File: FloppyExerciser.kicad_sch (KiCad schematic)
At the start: 112 parts, among them J1 STEPPER, J10 IBM 31SD, J11 PS/2, J12 APPLE II, J2 WRITE, J4 V, J5 ISP, J6 IBM, J7 HP 34-PIN, J8 HP 26-PIN, J9 SHUGART, SW1 RotaryEncoder_Switch, SW10 DIR, SW11 TG43 MODE, SW12 MENU, SW13 DENSITY, SW2 STEP, SW3 DISKCH_RST, SW4 DSEL, SW5 DSEL2, SW6 DRIVE_SELECT, SW7 MOTOR_ON, SW8 HEAD_SEL, SW9 HEAD_LOAD, U1 ATmega328PB-M, U2 74LS245, U3 74LS32, U4 74LS04

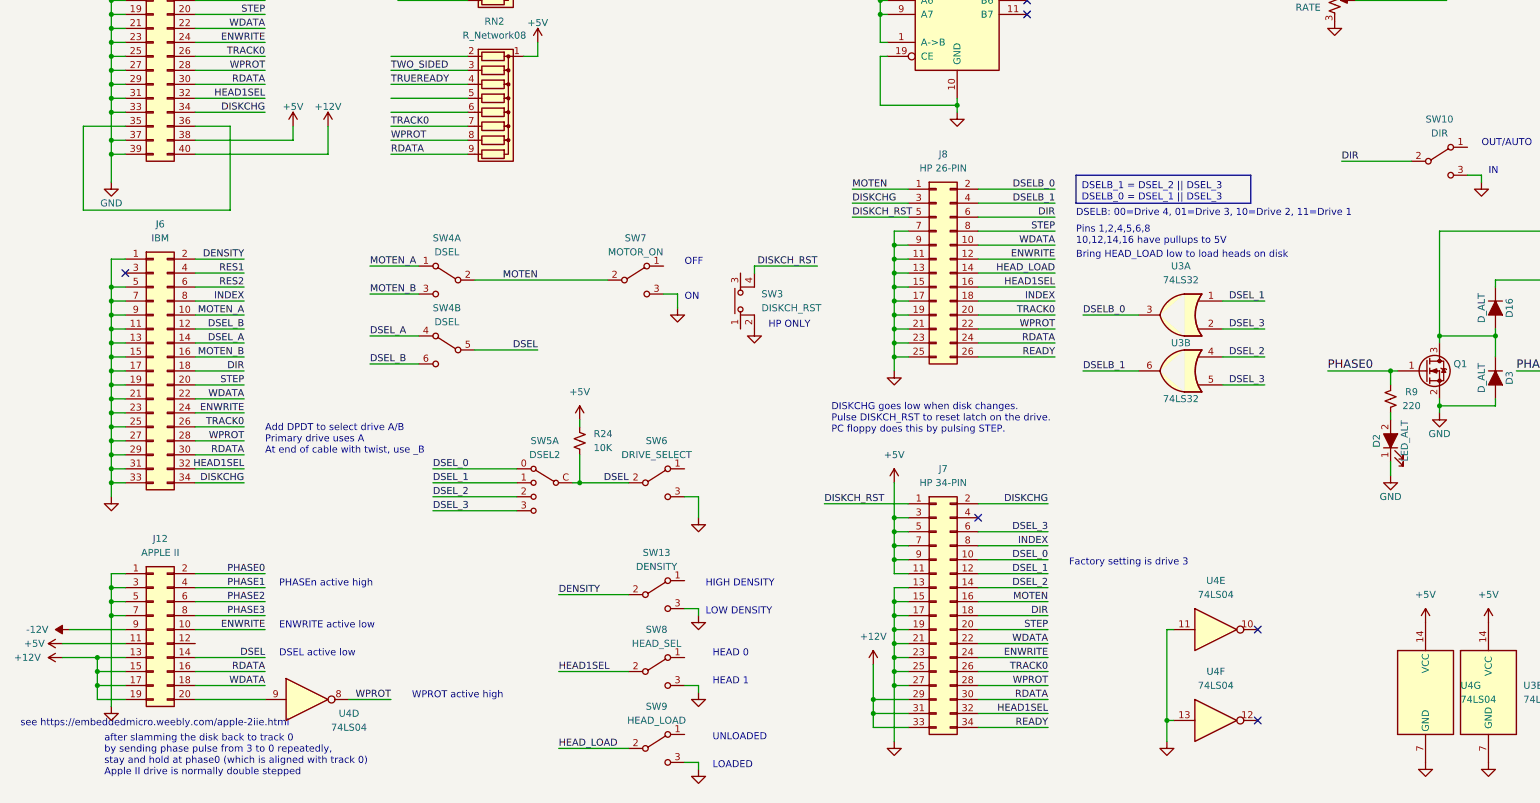
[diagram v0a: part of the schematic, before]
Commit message: Rev2 fab with minor fixes for HP 26 pin
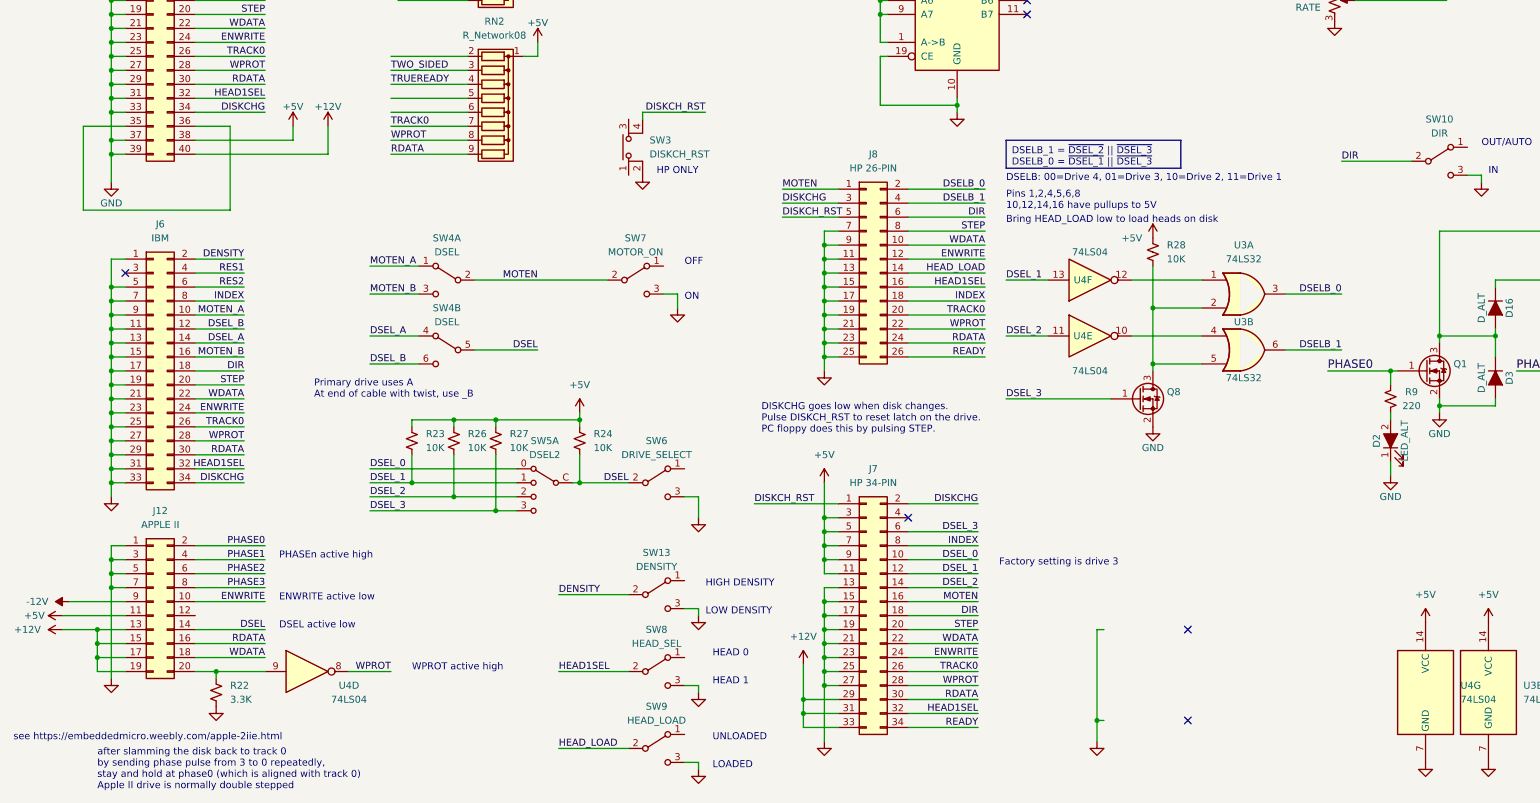
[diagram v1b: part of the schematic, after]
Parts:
- added Q8: ~, Active:SOT95P230X117-3, symbol SimpleStepper-rescue:Q_NMOS_GSD
- added R22: 3.3K, Passive:RESC1608X55, symbol Device:R_Small_US
- added R23, R26, R27, R28: 10K, Passive:RESC1608X55, symbol Device:R_Small_US
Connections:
- net +5V: now also R23.1, R26.1, R27.1, R28.1
- net DSEL_1: now also U4.13, R23.2; no longer U3.1
- net DSEL_2: now also U4.11, R26.2; no longer U3.4
- net DSEL_3: now also Q8.1 (G), R27.2; no longer U3.2, U3.5
- net GND: now also Q8.2 (S), R22.2; no longer U4.11, U4.13
- net at U4.12: now also U3.1
- net at J12.20 (Pin_20), U4.9: now also R22.1
- net at U4.10: now also U3.4
- new net: Q8.3 (D), R28.2, U3.2, U3.5
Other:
- note added: "Primary drive uses A At end of cable with twist, use _B"
- note removed: "Add DPDT to select drive A/B Primary drive uses A At end of cable with twist, use _B"
- moved on the sheet: J12, J7, J8, SW3, U3A, U3B, U4D, U4E, U4F

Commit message: Update readme, add fab and bom
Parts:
- D1: Digikey (none) -> LTD-2601G-11-ND; Mouser (none) -> 859-LTD-2601G-11
- D10, D11, D12, D13, D14, D15, D2, D4, D6, D8: Digikey (none) -> 160-1445-1-ND
- D16, D17, D18, D19, D3, D5, D7, D9: Digikey (none) -> ES1B-E3/61TGICT-ND
- R1, R10, R11, R23, R24, R25, R26, R27, R28: Digikey (none) -> RMCF0603JT10K0CT-ND
- R2, R3, R4, R5, R6, R7, R8, R9: Digikey (none) -> RMCF0603JT1K0CT-ND
- R22: Digikey (none) -> RMCF0603JT3K30CT-ND
- R9: Digikey (none) -> RMCF0603JT220RCT-ND
- RN1, RN2: Digikey (none) -> 4609X-101-102LF
- RV1: Digikey (none) -> 3386F-1-202TLF
- SW10, SW13, SW6, SW7, SW8, SW9: Digikey (none) -> 100SP1T1B4M2QE; Mouser 612-500-A122 -> (none)
- SW11: Digikey (none) -> 141-100DP6T3B4M2QE-ND
- SW12, SW2, SW3: Digikey (none) -> EG1828-ND
- SW4: Digikey (none) -> 100DP1T1B1M2QE
- SW5: Digikey (none) -> CT3098-ND
- TP1, TP10, TP11, TP12, TP13, TP14, TP15, TP16, TP17, TP18, TP19, TP2, TP20, TP21, TP22, TP23, TP24, TP25, TP3, TP4, TP5, TP6, TP7, TP8, TP9: Digikey (none) -> 36-5006-ND
- U1: Digikey (none) -> ATMEGA328PB-MU-ND
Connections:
- no-connect marks 11 -> 9
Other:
- note removed: "DP1: Negative sign?"
- note removed: "TODO: Double step switch, 2/3 step switch Maybe add menu buttons instead"

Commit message: Fix potentiometer part number
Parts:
- RV1: Digikey 3386F-1-202TLF -> 3386P-1-202TLF
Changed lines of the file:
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@@
       (effects (font (size 1.27 1.27)) hide)
     )
-    (property "Digikey" "3386F-1-202TLF" (at 255.27 138.43 0)
+    (property "Digikey" "3386P-1-202TLF" (at 255.27 138.43 0)
       (effects (font (size 1.27 1.27)) hide)
     )
@@
       (effects (font (size 1.27 1.27)) hide)
     )
-    (property "Digikey" "3386F-1-202TLF" (at 255.27 118.11 0)
-      (effects (font (size 1.27 1.27)) hide)
-    )
+    (property "Digikey" "3386P-1-202TLF" (at 255.27 118.11 0)
+      (effects (font (size 1.27 1.27)) hide)
+    )
+    (property "Mouser" "" (at 255.27 118.11 0)
+      (effects (font (size 1.27 1.27)) hide)
+    )
